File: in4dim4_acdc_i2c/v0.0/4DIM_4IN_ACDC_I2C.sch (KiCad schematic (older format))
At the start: 101 parts, among them IC1 ATTINY2313-P, IC2 MOC3021S, IC3 MOC3021S, IC4 MOC3021S, IC5 MOC3021S, IC6 P620, P10 CONN_2, P11 CONN_2, P12 CONN_2, P13 CONN_2, P14 CONN_2, P15 CONN_2, P4 CONN_5, P5 CONN_5, P6 CONN_5, P7 CONN_2, P8 CONN_2, P9 CONN_2, U1 TRIAC, U2 TRIAC, U3 TRIAC, U4 TRIAC

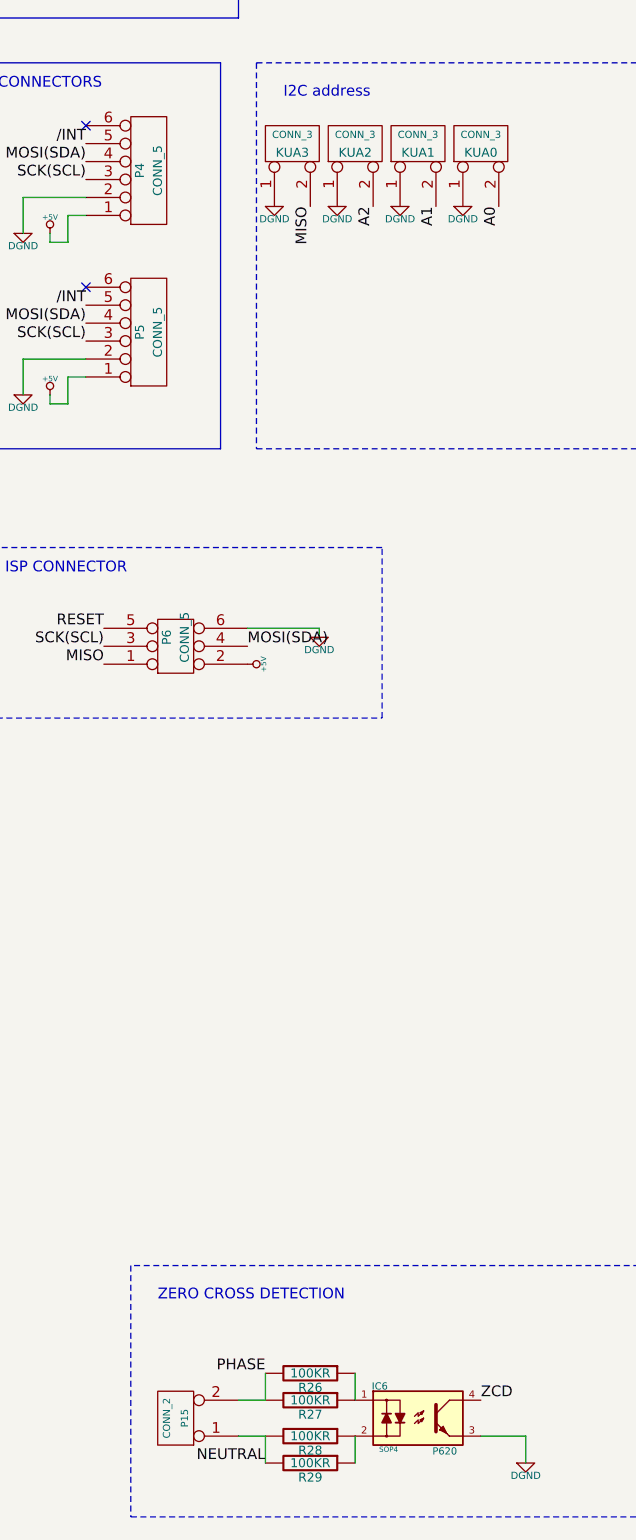
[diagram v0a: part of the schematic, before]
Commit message: Add 230VAC spare connector Change the position of leds inputs Generation of Gerber files
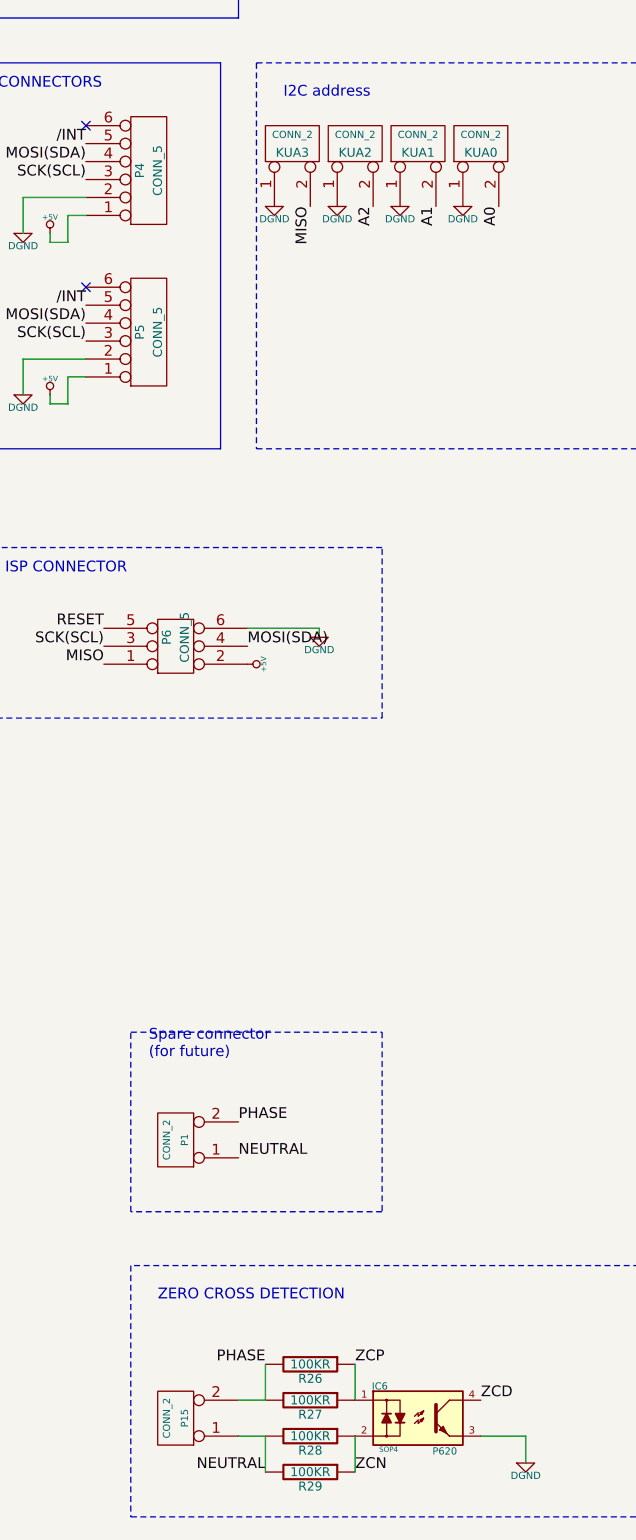
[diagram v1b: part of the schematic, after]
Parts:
- added P1: CONN_2, symbol CONN_2
- KUA0, KUA1, KUA2, KUA3: value CONN_3 -> CONN_2
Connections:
- net NEUTRAL: now also P1.1 (P1)
- net PHASE: now also P1.2 (PM)
- net ZCP: now reaches IC6.1, R26.1, R27.1
- net ZCN: now reaches IC6.2, R28.1, R29.1
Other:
- note added: "Spare connector\n(for future)"
- moved on the sheet: R26, R29
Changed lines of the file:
@@
-EESchema Schematic File Version 2  date mer. 19 sept. 2012 18:35:46 CEST
+EESchema Schematic File Version 2  date jeu. 20 sept. 2012 18:41:36 CEST
 LIBS:power
 LIBS:device
@@
 Sheet 1 1
 Title "4 inputs / 4 dimmers i2c board"
-Date "19 sep 2012"
+Date "20 sep 2012"
 Rev "0"
 Comp "XPLDUINO project"
@@
 $EndDescr
 $Comp
-L DGND #PWR01
+L DGND #PWR18
 U 1 1 4FA0F2DB
 P 6700 1800
-F 0 "#PWR01" H 6700 1800 40  0001 C CNN
+F 0 "#PWR18" H 6700 1800 40  0001 C CNN
 F 1 "DGND" H 6700 1730 40  0000 C CNN
 	1    6700 1800
@@
 $EndComp
 $Comp
-L +5V #PWR02
+L +5V #PWR17
 U 1 1 4FA0F021
 P 6700 900
-F 0 "#PWR02" H 6700 990 20  0001 C CNN
+F 0 "#PWR17" H 6700 990 20  0001 C CNN
 F 1 "+5V" H 6700 990 30  0000 C CNN
 	1    6700 900
@@
 $EndComp
 $Comp
-L DGND #PWR03
+L DGND #PWR3
 U 1 1 4F8D1920
 P 2700 9650
-F 0 "#PWR03" H 2700 9650 40  0001 C CNN
+F 0 "#PWR3" H 2700 9650 40  0001 C CNN
 F 1 "DGND" H 2700 9580 40  0000 C CNN
 	1    2700 9650
@@
 $EndComp
 $Comp
-L DGND #PWR04
+L DGND #PWR10
 U 1 1 4F8D191C
 P 5900 3300
-F 0 "#PWR04" H 5900 3300 40  0001 C CNN
+F 0 "#PWR10" H 5900 3300 40  0001 C CNN
 F 1 "DGND" H 5900 3230 40  0000 C CNN
 	1    5900 3300
@@
 $EndComp
 $Comp
-L DGND #PWR05
+L DGND #PWR24
 U 1 1 4F8D190F
 P 8350 3150
-F 0 "#PWR05" H 8350 3150 40  0001 C CNN
+F 0 "#PWR24" H 8350 3150 40  0001 C CNN
 F 1 "DGND" H 8350 3080 40  0000 C CNN
 	1    8350 3150
@@
 $EndComp
 $Comp
-L DGND #PWR06
+L DGND #PWR23
 U 1 1 4F8D190C
 P 8000 3150
-F 0 "#PWR06" H 8000 3150 40  0001 C CNN
+F 0 "#PWR23" H 8000 3150 40  0001 C CNN
 F 1 "DGND" H 8000 3080 40  0000 C CNN
 	1    8000 3150
@@
 $EndComp
 $Comp
-L DGND #PWR07
+L DGND #PWR22
 U 1 1 4F8D1909
 P 7650 3150
-F 0 "#PWR07" H 7650 3150 40  0001 C CNN
+F 0 "#PWR22" H 7650 3150 40  0001 C CNN
 F 1 "DGND" H 7650 3080 40  0000 C CNN
 	1    7650 3150
@@
 P 8100 2800
 F 0 "KUA1" V 8050 2800 50  0000 C CNN
-F 1 "CONN_3" V 8150 2800 40  0000 C CNN
+F 1 "CONN_2" V 8150 2800 40  0000 C CNN
 	1    8100 2800
 	0    -1   -1   0
@@
 P 8450 2800
 F 0 "KUA0" V 8400 2800 50  0000 C CNN
-F 1 "CONN_3" V 8500 2800 40  0000 C CNN
+F 1 "CONN_2" V 8500 2800 40  0000 C CNN
 	1    8450 2800
 	0    -1   -1   0
@@
 P 7750 2800
 F 0 "KUA2" V 7700 2800 50  0000 C CNN
-F 1 "CONN_3" V 7800 2800 40  0000 C CNN
+F 1 "CONN_2" V 7800 2800 40  0000 C CNN
 	1    7750 2800
 	0    -1   -1   0
 $EndComp
 $Comp
-L DGND #PWR08
+L DGND #PWR4
 U 1 1 4F8AE822
 P 4500 2150
-F 0 "#PWR08" H 4500 2150 40  0001 C CNN
+F 0 "#PWR4" H 4500 2150 40  0001 C CNN
 F 1 "DGND" H 4500 2080 40  0000 C CNN
 	1    4500 2150
@@
 $EndComp
 $Comp
-L DGND #PWR09
+L DGND #PWR5
 U 1 1 4F8AE820
 P 4500 3250
-F 0 "#PWR09" H 4500 3250 40  0001 C CNN
+F 0 "#PWR5" H 4500 3250 40  0001 C CNN
 F 1 "DGND" H 4500 3180 40  0000 C CNN
 	1    4500 3250
@@
 $EndComp
 $Comp
-L DGND #PWR010
+L DGND #PWR7
 U 1 1 4F8AE7F9
 P 4550 5850
-F 0 "#PWR010" H 4550 5850 40  0001 C CNN
+F 0 "#PWR7" H 4550 5850 40  0001 C CNN
 F 1 "DGND" H 4550 5780 40  0000 C CNN
 	1    4550 5850
@@
 MOSI(SDA)
 $Comp
-L VCC #PWR011
+L VCC #PWR12
 U 1 1 4F81ECBF
 P 6000 1100
-F 0 "#PWR011" H 6000 1200 30  0001 C CNN
+F 0 "#PWR12" H 6000 1200 30  0001 C CNN
 F 1 "VCC" H 6000 1200 30  0000 C CNN
 	1    6000 1100
@@
 $EndComp
 $Comp
-L +5V #PWR012
+L +5V #PWR15
 U 1 1 4F81B238
 P 6150 1100
-F 0 "#PWR012" H 6150 1190 20  0001 C CNN
+F 0 "#PWR15" H 6150 1190 20  0001 C CNN
 F 1 "+5V" H 6150 1190 30  0000 C CNN
 	1    6150 1100
@@
 $EndComp
 $Comp
-L +5V #PWR013
+L +5V #PWR13
 U 1 1 4F81B068
 P 6050 3300
-F 0 "#PWR013" H 6050 3390 20  0001 C CNN
+F 0 "#PWR13" H 6050 3390 20  0001 C CNN
 F 1 "+5V" H 6050 3390 30  0000 C CNN
 	1    6050 3300
@@
 IN1
 $Comp
-L PWR_FLAG #FLG014
+L PWR_FLAG #FLG1
 U 1 1 4F8011B6
 P 5800 1150
-F 0 "#FLG014" H 5800 1245 30  0001 C CNN
+F 0 "#FLG1" H 5800 1245 30  0001 C CNN
 F 1 "PWR_FLAG" H 5800 1330 30  0000 C CNN
 	1    5800 1150
@@
 A2
 $Comp
-L +5V #PWR015
+L +5V #PWR2
 U 1 1 502AAFBD
 P 2700 7550
-F 0 "#PWR015" H 2700 7640 20  0001 C CNN
+F 0 "#PWR2" H 2700 7640 20  0001 C CNN
 F 1 "+5V" H 2700 7640 30  0000 C CNN
 	1    2700 7550
@@
 $EndComp
 $Comp
-L +5V #PWR016
+L +5V #PWR26
 U 1 1 502AB423
 P 10600 1050
-F 0 "#PWR016" H 10600 1140 20  0001 C CNN
+F 0 "#PWR26" H 10600 1140 20  0001 C CNN
 F 1 "+5V" H 10600 1140 30  0000 C CNN
 	1    10600 1050
@@
 $EndComp
 $Comp
-L +5V #PWR017
+L +5V #PWR27
 U 1 1 502ABA18
 P 10600 3000
-F 0 "#PWR017" H 10600 3090 20  0001 C CNN
+F 0 "#PWR27" H 10600 3090 20  0001 C CNN
 F 1 "+5V" H 10600 3090 30  0000 C CNN
 	1    10600 3000
@@
 $EndComp
 $Comp
-L +5V #PWR018
+L +5V #PWR28
 U 1 1 502ABA5E
 P 10600 5100
-F 0 "#PWR018" H 10600 5190 20  0001 C CNN
+F 0 "#PWR28" H 10600 5190 20  0001 C CNN
 F 1 "+5V" H 10600 5190 30  0000 C CNN
 	1    10600 5100
@@
 $EndComp
 $Comp
-L +5V #PWR019
+L +5V #PWR29
 U 1 1 502ABAA4
 P 10600 7050
-F 0 "#PWR019" H 10600 7140 20  0001 C CNN
+F 0 "#PWR29" H 10600 7140 20  0001 C CNN
 F 1 "+5V" H 10600 7140 30  0000 C CNN
 	1    10600 7050
@@
 DIM3
 $Comp
-L DGND #PWR020
+L DGND #PWR11
 U 1 1 502B5AF8
 P 5900 4200
-F 0 "#PWR020" H 5900 4200 40  0001 C CNN
+F 0 "#PWR11" H 5900 4200 40  0001 C CNN
 F 1 "DGND" H 5900 4130 40  0000 C CNN
 	1    5900 4200
@@
 MOSI(SDA)
 $Comp
-L +5V #PWR021
+L +5V #PWR14
 U 1 1 502B5B07
 P 6050 4200
-F 0 "#PWR021" H 6050 4290 20  0001 C CNN
+F 0 "#PWR14" H 6050 4290 20  0001 C CNN
 F 1 "+5V" H 6050 4290 30  0000 C CNN
 	1    6050 4200
@@
 RESET
 $Comp
-L DGND #PWR022
+L DGND #PWR21
 U 1 1 502BFAB3
 P 7550 5550
-F 0 "#PWR022" H 7550 5550 40  0001 C CNN
+F 0 "#PWR21" H 7550 5550 40  0001 C CNN
 F 1 "DGND" H 7550 5480 40  0000 C CNN
 	1    7550 5550
@@
 $EndComp
 $Comp
-L +5V #PWR023
+L +5V #PWR19
 U 1 1 502BFAB9
 P 7150 5700
-F 0 "#PWR023" H 7150 5790 20  0001 C CNN
+F 0 "#PWR19" H 7150 5790 20  0001 C CNN
 F 1 "+5V" H 7150 5790 30  0000 C CNN
 	1    7150 5700
@@
 $EndComp
 $Comp
-L +5V #PWR024
+L +5V #PWR1
 U 1 1 502BFC90
 P 1550 7100
-F 0 "#PWR024" H 1550 7190 20  0001 C CNN
+F 0 "#PWR1" H 1550 7190 20  0001 C CNN
 F 1 "+5V" H 1550 7190 30  0000 C CNN
 	1    1550 7100
@@
 L R R26
 U 1 1 502FC419
-P 7500 9650
-F 0 "R26" V 7580 9650 50  0000 C CNN
-F 1 "100KR" V 7500 9650 50  0000 C CNN
-	1    7500 9650
+P 7500 9600
+F 0 "R26" V 7580 9600 50  0000 C CNN
+F 1 "100KR" V 7500 9600 50  0000 C CNN
+	1    7500 9600
 	0    1    1    0
 $EndComp
@@
 L R R29
 U 1 1 502FC425
-P 7500 10150
-F 0 "R29" V 7580 10150 50  0000 C CNN
-F 1 "100KR" V 7500 10150 50  0000 C CNN
-	1    7500 10150
+P 7500 10200
+F 0 "R29" V 7580 10200 50  0000 C CNN
+F 1 "100KR" V 7500 10200 50  0000 C CNN
+	1    7500 10200
 	0    1    1    0
 $EndComp
 $Comp
-L DGND #PWR025
+L DGND #PWR25
 U 1 1 502FC913
 P 8700 10150
-F 0 "#PWR025" H 8700 10150 40  0001 C CNN
+F 0 "#PWR25" H 8700 10150 40  0001 C CNN
 F 1 "DGND" H 8700 10080 40  0000 C CNN
 	1    8700 10150
@@
 Text Notes 6650 9250 0    60   ~ 0
 ZERO CROSS DETECTION
-Text Label 7250 9650 2    60   ~ 0
+Text Label 7250 9600 2    60   ~ 0
 PHASE
-Text Label 7250 10150 2    60   ~ 0
+Text Label 7250 10200 2    60   ~ 0
 NEUTRAL
 Text Label 11350 1450 0    60   ~ 0
@@
 LED
 $Comp
-L DGND #PWR026
+L DGND #PWR8
 U 1 1 50354366
 P 4650 10200
-F 0 "#PWR026" H 4650 10200 40  0001 C CNN
+F 0 "#PWR8" H 4650 10200 40  0001 C CNN
 F 1 "DGND" H 4650 10130 40  0000 C CNN
 	1    4650 10200
@@
 $EndComp
 $Comp
-L DGND #PWR027
+L DGND #PWR20
 U 1 1 503E5DD9
 P 7300 3150
-F 0 "#PWR027" H 7300 3150 40  0001 C CNN
+F 0 "#PWR20" H 7300 3150 40  0001 C CNN
 F 1 "DGND" H 7300 3080 40  0000 C CNN
 	1    7300 3150
@@
 P 7400 2800
 F 0 "KUA3" V 7350 2800 50  0000 C CNN
-F 1 "CONN_3" V 7450 2800 40  0000 C CNN
+F 1 "CONN_2" V 7450 2800 40  0000 C CNN
 	1    7400 2800
 	0    -1   -1   0
@@
 $EndComp
 $Comp
-L DGND #PWR028
+L DGND #PWR16
 U 1 1 50479B59
 P 6150 1800
-F 0 "#PWR028" H 6150 1800 40  0001 C CNN
+F 0 "#PWR16" H 6150 1800 40  0001 C CNN
 F 1 "DGND" H 6150 1730 40  0000 C CNN
 	1    6150 1800
@@
 $EndComp
 $Comp
-L DGND #PWR029
+L DGND #PWR9
 U 1 1 50479B5F
 P 5800 1800
-F 0 "#PWR029" H 5800 1800 40  0001 C CNN
+F 0 "#PWR9" H 5800 1800 40  0001 C CNN
 F 1 "DGND" H 5800 1730 40  0000 C CNN
 	1    5800 1800
@@
 	14250 7250 14200 7250
 Wire Wire Line
-	7250 9800 7250 9650
-Wire Wire Line
-	7750 9650 7750 9800
-Wire Wire Line
-	7750 10150 7750 10000
-Wire Wire Line
-	7250 10150 7250 10000
+	7250 9600 7250 9800
+Wire Wire Line
+	7750 9600 7750 9800
+Wire Wire Line
+	7750 10000 7750 10200
+Wire Wire Line
+	7250 10000 7250 10200
 Wire Wire Line
 	8450 10000 8700 10000
@@
 	9600 9050 6500 9050
 Wire Wire Line
-	7100 9800 7250 9800
+	7250 9800 7100 9800
 Wire Wire Line
 	7250 10000 7100 10000
@@
 Connection ~ 1850 3650
 $Comp
-L DGND #PWR030
+L DGND #PWR6
 U 1 1 5059C700
 P 4550 4550
-F 0 "#PWR030" H 4550 4550 40  0001 C CNN
+F 0 "#PWR6" H 4550 4550 40  0001 C CNN
 F 1 "DGND" H 4550 4480 40  0000 C CNN
 	1    4550 4550
 	1    0    0    -1
 $EndComp
+$Comp
+L CONN_2 P1
+U 1 1 505B4875
+P 6750 8350
+F 0 "P1" V 6700 8350 40  0000 C CNN
+F 1 "CONN_2" V 6800 8350 40  0000 C CNN
+	1    6750 8350
+	-1   0    0    1
+$EndComp
+Text Label 7100 8250 0    60   ~ 0
+PHASE
+Text Label 7100 8450 0    60   ~ 0
+NEUTRAL
+Wire Notes Line
+	6500 8750 6500 7750
+Wire Notes Line
+	6500 7750 7900 7750
+Wire Notes Line
+	7900 7750 7900 8750
+Wire Notes Line
+	7900 8750 6500 8750
+Text Notes 6600 7900 0    60   ~ 0
+Spare connector\n(for future)
+Text Label 7750 9600 0    60   ~ 0
+ZCP
+Text Label 7750 10200 0    60   ~ 0
+ZCN
 $EndSCHEMATC
